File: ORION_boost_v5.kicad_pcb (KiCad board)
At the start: 4 copper layers, 87.5 x 119 mm, 154 parts, among them J1 Conn_02x04_Odd_Even, J10 Conn_01x01, J11 Conn_01x01, J2 Conn_01x10, J3 Conn_01x03, J4 Conn_01x03, J5 Conn_01x01, J6 Conn_01x01, J7 Conn_01x02, J8 Conn_01x02, J9 Conn_01x02, P1 CONN_01X06, P2 CONN_01X02, P3 CONN_01X02, P4 CONN_01X02, P5 CONN_01X02, P6 CONN_01X02, P7 CONN_01X02, Q1 Q_NMOS_GDS, Q10 Q_NMOS_GSD, Q2 Q_NMOS_GDS, Q3 Q_NMOS_GSD, Q4 Q_PMOS_GDS, Q5 Q_NMOS_GDS, Q6 Q_NMOS_GDS, Q7 Q_NMOS_GDS, Q8 Q_NMOS_GDS, Q9 Q_NMOS_GDS, SW1 SW_Push, SW2 SW_Push, SW3 SW_Push, SW4 SW_Push, U1 STM32F303CBTx, U2 MAX3051, U3 ZXCT108x, X1 ceralock

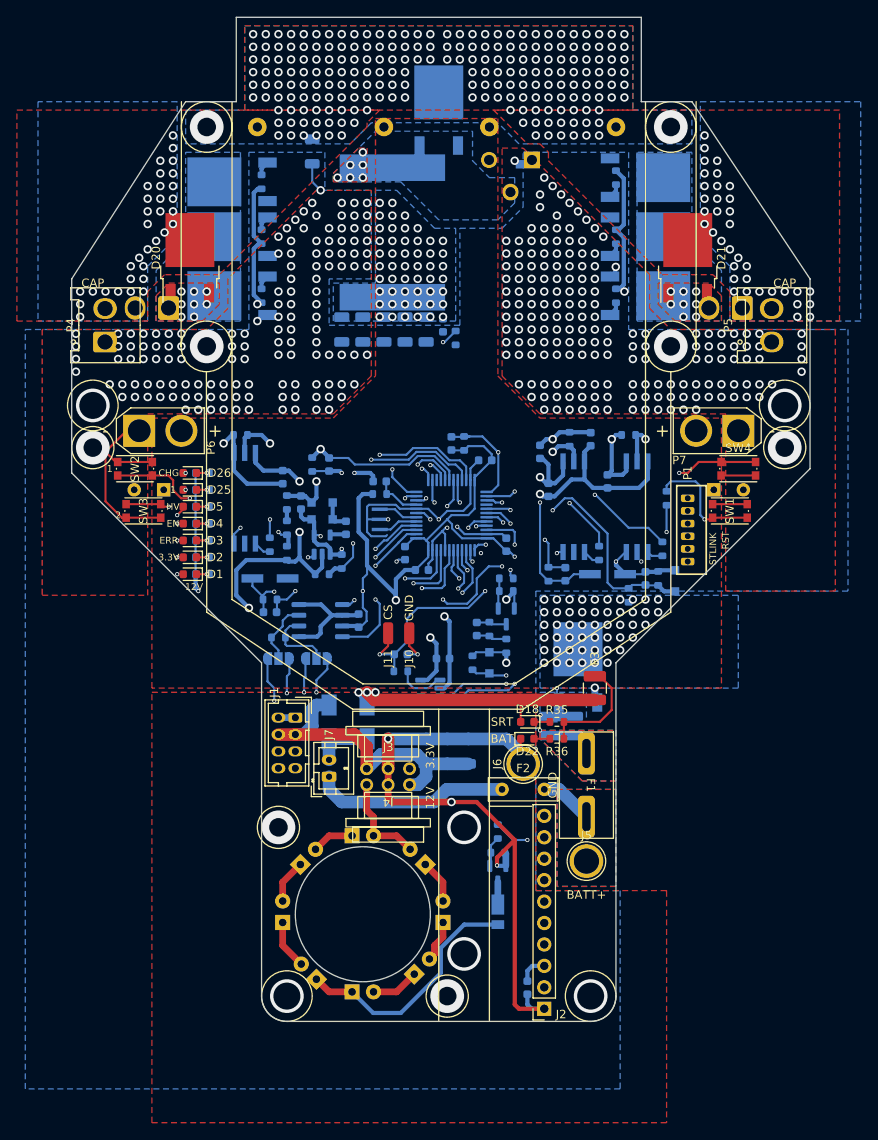
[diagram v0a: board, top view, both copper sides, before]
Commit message: KiCAD8.0に更新
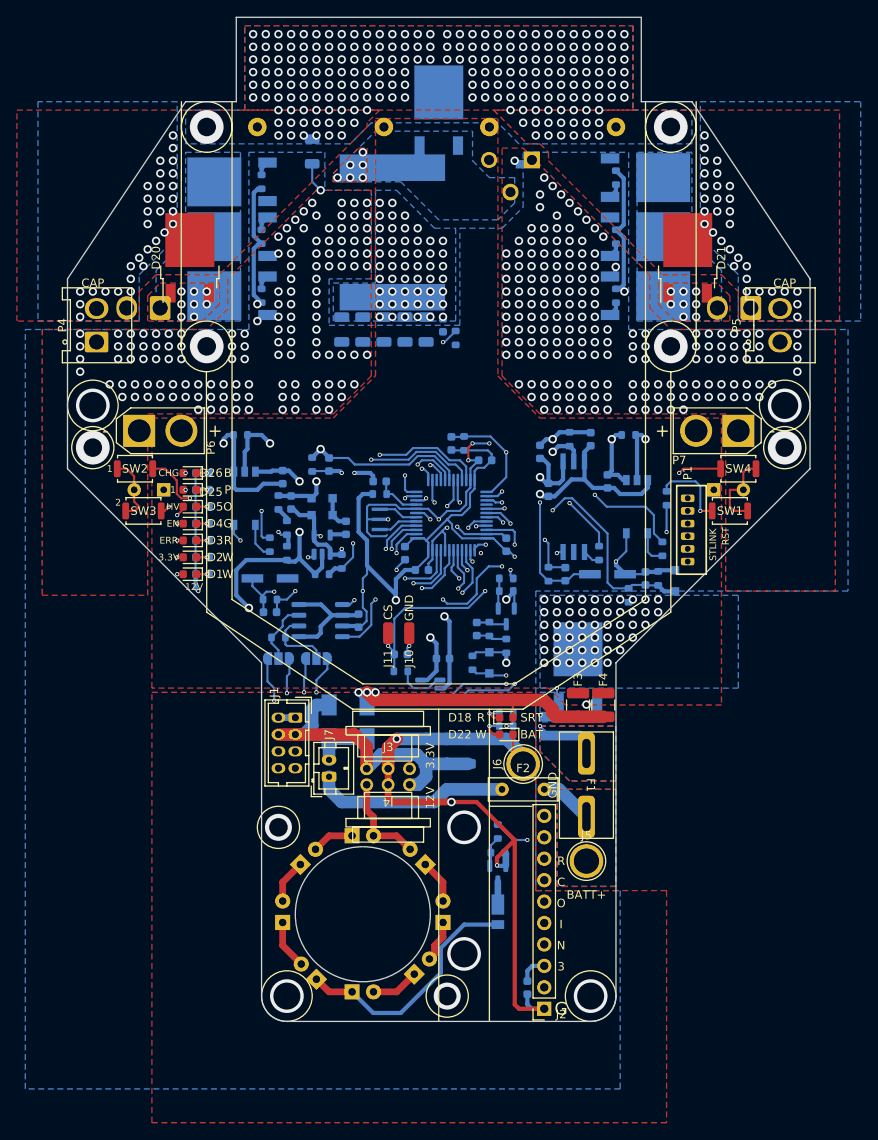
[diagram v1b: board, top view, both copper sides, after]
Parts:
- removed FB1: FerriteBead, Resistor_SMD:R_0603_1608Metric
- added F4: Fuse, Fuse:Fuse_1210_3225Metric, F.Cu at (144.5, 121.5)
- added R45: 1, Resistor_SMD:R_0603_1608Metric, B.Cu at (118.0, 96.5)
- PC1, PC2: footprint Package_SO:SSO-6_6.8x4.6mm_P1.27mm_Clearance8mm -> Package_SO:MFSOP6-5_4.4x3.6mm_P1.27mm
- R35, R36: moved to B.Cu
- SW1, SW2, SW3, SW4: footprint Button_Switch_SMD:SW_Push_1P1T_NO_CK_KMR2 -> Button_Switch_SMD:SW_Push_SPST_NO_Alps_SKRK
- moved R36 6.18 mm to (133.0, 124.0)
- moved R35 6.08 mm to (133.0, 122.5)
- moved F3 2.83 mm to (141.5, 121.5)
- moved D18 2.55 mm to (133.0, 123.0), turned to 0 degrees
- moved D22 2.55 mm to (133.0, 125.0), turned to 180 degrees
- moved C31 1.17 mm to (107.5, 97.5)
- moved P2 1.00 mm to (92.0, 74.5)
- moved P3 1.00 mm to (162.0, 74.5)
- moved P4 1.00 mm to (84.5, 78.5)
- moved P5 1.00 mm to (165.4, 78.5)
- moved R20 1.00 mm to (106.0, 97.5)
- moved D23 0.50 mm to (111.2, 99.0)
- moved D24 0.50 mm to (111.2, 97.0)
- turned SW1 to 0 degrees
- turned SW3 to 180 degrees
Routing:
- net +BATT: track 44.0 -> 52.2 mm, vias 101 -> 102
- net GND: track 360.1 -> 352.9 mm, vias 339 -> 338
- net /NRST: track 54.4 -> 48.3 mm
- net /SW_3: track 35.6 -> 31.2 mm
- net /SW_2: track 48.0 -> 43.9 mm
- net /SW_1: track 54.4 -> 50.4 mm
- net +12V: track 139.3 -> 136.7 mm
- net Net-(PC1-Pad1): track 2.10 -> 4.32 mm
- net /KICK_2_GATE: track 38.5 -> 40.8 mm
- net /KICK_1_GATE: track 41.1 -> 43.3 mm
- net Net-(PC2-Pad1): track 1.92 -> 4.14 mm
- net /KICK_2_SOURCE: track 30.8 -> 32.9 mm
- net Net-(C21-Pad2): track 52.2 -> 50.6 mm
- net Net-(D18-Pad2): track 33.9 -> 35.6 mm
- net /GD_16M: track 27.3 -> 28.6 mm
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- removed copper zone on In2.Cu, net Net-(D19-Pad2)
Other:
- board size 87.5 x 119 mm -> 88 x 119 mm
- board text added: "12V G IN"
- board text added: "2024/09/13 designed by ibis"
- board text added: "3"
- board text added: "3V3 G IN"
- board text added: "B"
- board text added: "C"
- board text added: "G"
- board text added: "I"
- board text added: "Logic"
- board text added: "N"
- board text added: "O"
- board text added: "P"
- board text added: "PreChg"
- board text added: "R"
- board text added: "W"
- board text removed: "2023/05/20 designed by ibis"

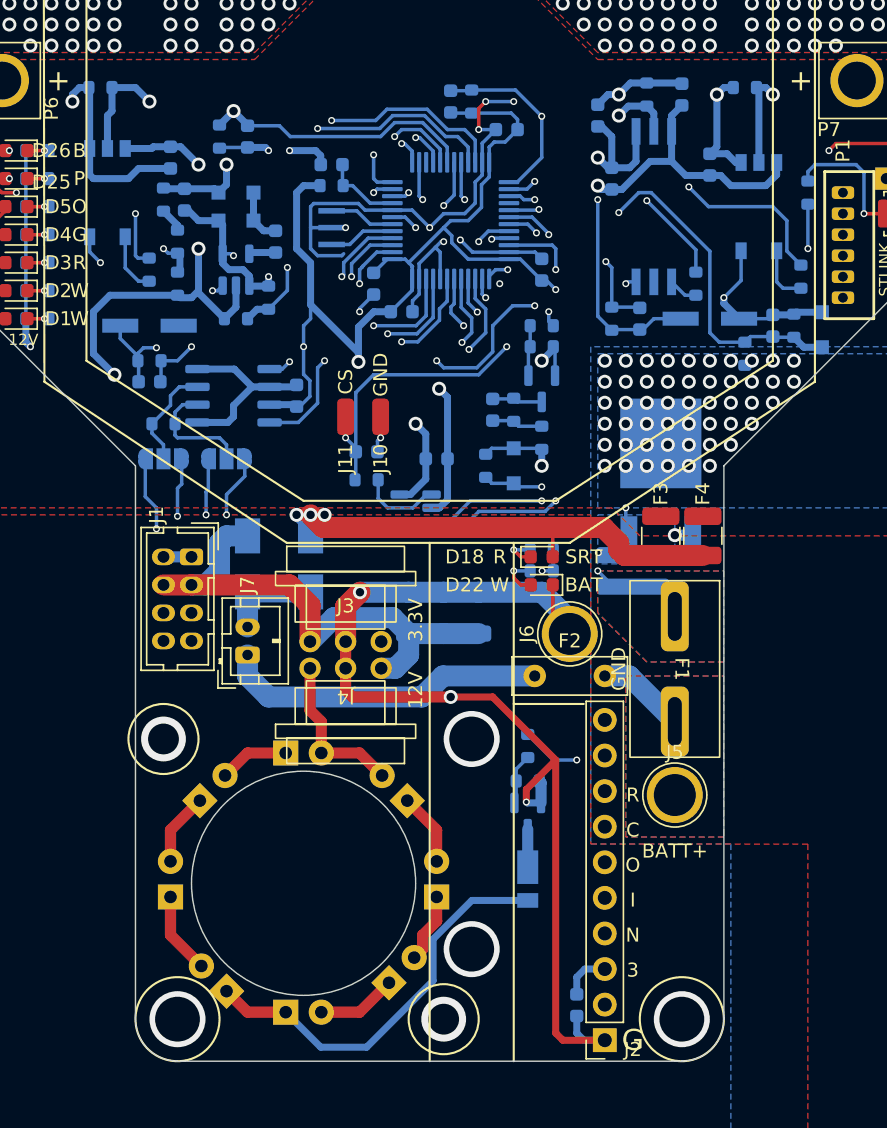
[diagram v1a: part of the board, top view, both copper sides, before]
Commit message: KiCAD8に更新
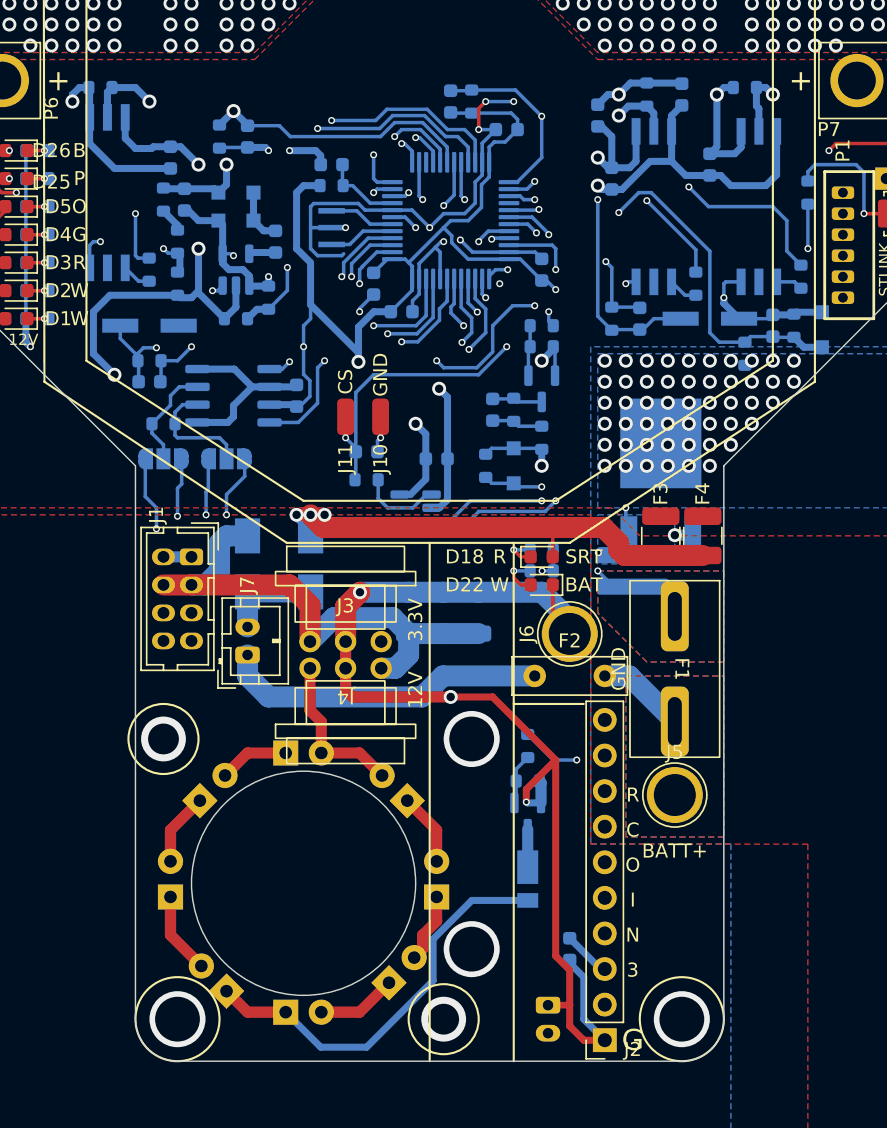
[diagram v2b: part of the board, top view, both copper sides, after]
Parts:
- added J12: Conn_01x02, Connector_JST:JST_PH_B2B-PH-K_1x02_P2.00mm_Vertical, B.Cu at (133.4, 155.0)
- PC1, PC2: footprint Package_SO:MFSOP6-5_4.4x3.6mm_P1.27mm -> Package_SO:SSO-6_6.8x4.6mm_P1.27mm_Clearance8mm
- moved C8 4.03 mm to (135.0, 151.0)
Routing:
- net /LOGIC_POWER: track 37.4 -> 69.4 mm
- net GND: track 352.9 -> 357.1 mm
- net +12V: track 136.7 -> 140.8 mm
- net Net-(PC2-A): track 4.14 -> 1.92 mm
- net Net-(PC1-A): track 4.32 -> 2.10 mm
- net /KICK_2_GATE: track 40.8 -> 38.5 mm
- net /KICK_1_GATE: track 43.3 -> 41.4 mm
- net /KICK_2_SOURCE: track 32.9 -> 31.0 mm
- net +3.3V: track 194.6 -> 193.4 mm
- net /KICK_1_SOURCE: track 30.1 -> 31.1 mm
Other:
- board text added: "2024/11/17 designed by ibis"
- board text removed: "2024/09/13 designed by ibis"
